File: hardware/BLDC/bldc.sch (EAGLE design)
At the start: 83 parts, among them J1 PWR_2_XT30PW-M, J2 LINEAR_35040500391, J3 LINEAR_8530480810, U1 MA702, U10 MCP2542FD, U11 LDFM33PUR, U2 DRV8323RS, U3 TPN7R006PL, U4 TPN7R006PL, U5 TPN7R006PL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

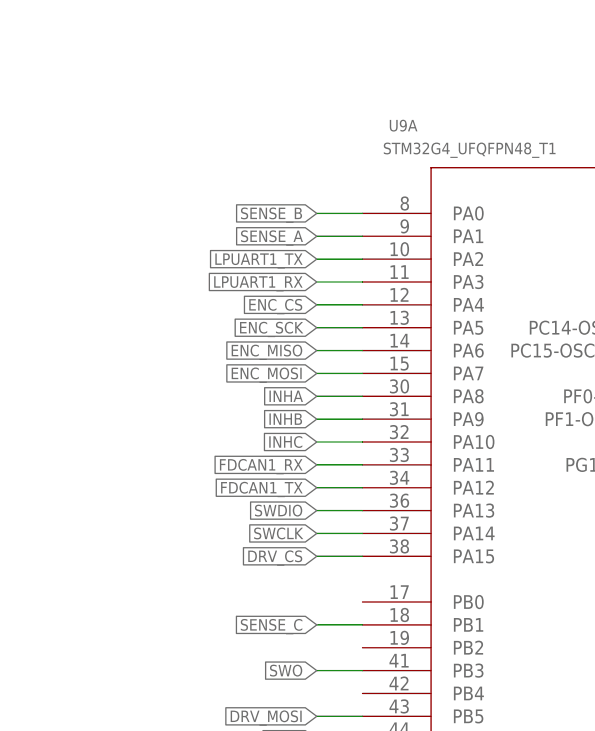
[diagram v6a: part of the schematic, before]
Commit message: Add pullups to SPI NSS pins
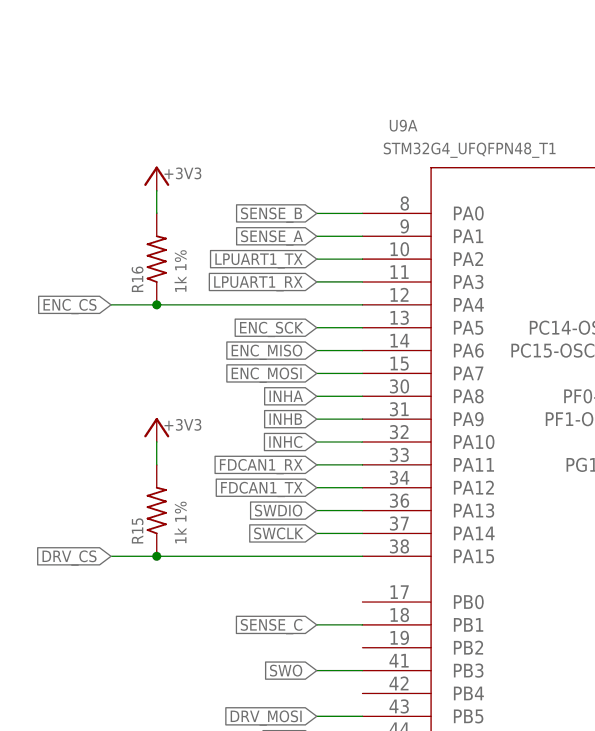
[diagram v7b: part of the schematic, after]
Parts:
- added R15, R16: 1k 1%, _T_rcl:R0402
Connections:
- net +3V3: now also R15.2, R16.2
- net DRV_CS: now also R15.1
- net ENC_CS: now also R16.1
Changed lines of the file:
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@@
 <part name="C43" library="_T_rcl" library_urn="urn:adsk.eagle:library:19571919" deviceset="C" device="0402" package3d_urn="urn:adsk.eagle:package:19572013/4" value="0.1uF 10V"/>
 <part name="GND31" library="_T_power" library_urn="urn:adsk.eagle:library:19572085" deviceset="GND" device=""/>
+<part name="R15" library="_T_rcl" library_urn="urn:adsk.eagle:library:19571919" deviceset="R" device="0402" package3d_urn="urn:adsk.eagle:package:19572014/3" value="1k 1%"/>
+<part name="+3V6" library="_T_power" library_urn="urn:adsk.eagle:library:19572085" deviceset="+3V3" device=""/>
+<part name="R16" library="_T_rcl" library_urn="urn:adsk.eagle:library:19571919" deviceset="R" device="0402" package3d_urn="urn:adsk.eagle:package:19572014/3" value="1k 1%"/>
+<part name="+3V7" library="_T_power" library_urn="urn:adsk.eagle:library:19572085" deviceset="+3V3" device=""/>
 </parts>
 <sheets>
@@
 </instance>
 <instance part="GND31" gate="G$1" x="17.78" y="-20.32" smashed="yes" grouprefs="UCPOWER"/>
+<instance part="R15" gate="G$1" x="-81.28" y="91.44" smashed="yes" rot="R90">
+<attribute name="NAME" x="-82.7786" y="87.63" size="1.27" layer="95" rot="R90"/>
+<attribute name="VALUE" x="-77.978" y="87.63" size="1.27" layer="96" rot="R90"/>
+</instance>
+<instance part="+3V6" gate="G$1" x="-81.28" y="101.6" smashed="yes">
+<attribute name="VALUE" x="-76.2" y="101.6" size="1.27" layer="96" rot="R180"/>
+</instance>
+<instance part="R16" gate="G$1" x="-81.28" y="119.38" smashed="yes" rot="R90">
+<attribute name="NAME" x="-82.7786" y="115.57" size="1.27" layer="95" rot="R90"/>
+<attribute name="VALUE" x="-77.978" y="115.57" size="1.27" layer="96" rot="R90"/>
+</instance>
+<instance part="+3V7" gate="G$1" x="-81.28" y="129.54" smashed="yes">
+<attribute name="VALUE" x="-76.2" y="129.54" size="1.27" layer="96" rot="R180"/>
+</instance>
 </instances>
 <busses>
@@
 <junction x="17.78" y="-7.62" grouprefs="UCPOWER"/>
 </segment>
+<segment>
+<wire x1="-81.28" y1="99.06" x2="-81.28" y2="96.52" width="0.1524" layer="91"/>
+<pinref part="+3V6" gate="G$1" pin="+3V3"/>
+<pinref part="R15" gate="G$1" pin="2"/>
+</segment>
+<segment>
+<wire x1="-81.28" y1="127" x2="-81.28" y2="124.46" width="0.1524" layer="91"/>
+<pinref part="+3V7" gate="G$1" pin="+3V3"/>
+<pinref part="R16" gate="G$1" pin="2"/>
+</segment>
 </net>
 <net name="N$1" class="0">
@@
 <segment>
 <pinref part="U9" gate="A" pin="PA15"/>
-<wire x1="-58.42" y1="86.36" x2="-63.5" y2="86.36" width="0.1524" layer="91" grouprefs="UC_STM32G4"/>
-<label x="-63.5" y="86.36" size="1.27" layer="95" rot="R180" xref="yes" grouprefs="UC_STM32G4"/>
+<wire x1="-58.42" y1="86.36" x2="-81.28" y2="86.36" width="0.1524" layer="91" grouprefs="UC_STM32G4"/>
+<label x="-86.36" y="86.36" size="1.27" layer="95" rot="R180" xref="yes" grouprefs="UC_STM32G4"/>
+<pinref part="R15" gate="G$1" pin="1"/>
+<wire x1="-81.28" y1="86.36" x2="-86.36" y2="86.36" width="0.1524" layer="91" grouprefs="UC_STM32G4"/>
+<junction x="-81.28" y="86.36"/>
 </segment>
 </net>
@@
 <segment>
 <pinref part="U9" gate="A" pin="PA4"/>
-<wire x1="-58.42" y1="114.3" x2="-63.5" y2="114.3" width="0.1524" layer="91" grouprefs="UC_STM32G4"/>
-<label x="-63.5" y="114.3" size="1.27" layer="95" rot="R180" xref="yes" grouprefs="UC_STM32G4"/>
-</segment>
-</net>
+<wire x1="-58.42" y1="114.3" x2="-81.28" y2="114.3" width="0.1524" layer="91" grouprefs="UC_STM32G4"/>
+<label x="-86.36" y="114.3" size="1.27" layer="95" rot="R180" xref="yes" grouprefs="UC_STM32G4"/>
+<pinref part="R16" gate="G$1" pin="1"/>
+<wire x1="-81.28" y1="114.3" x2="-86.36" y2="114.3" width="0.1524" layer="91" grouprefs="UC_STM32G4"/>
+<junction x="-81.28" y="114.3"/>
+</segment>
+</net>

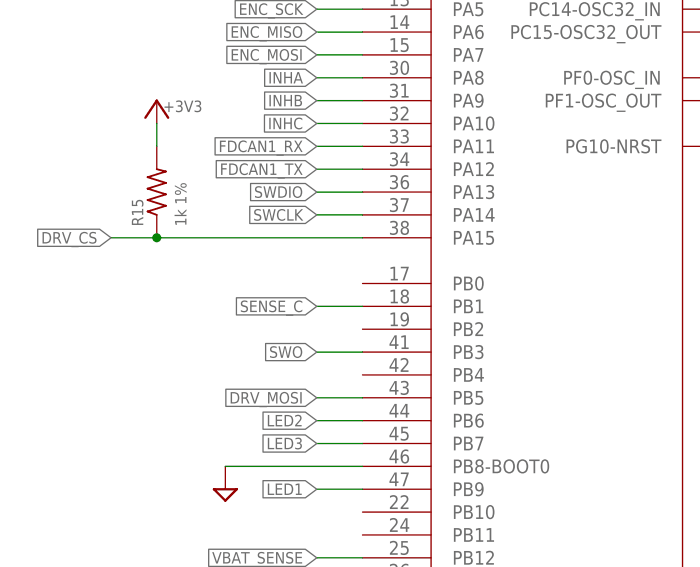
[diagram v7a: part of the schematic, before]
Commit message: Added nfault connection to PB0
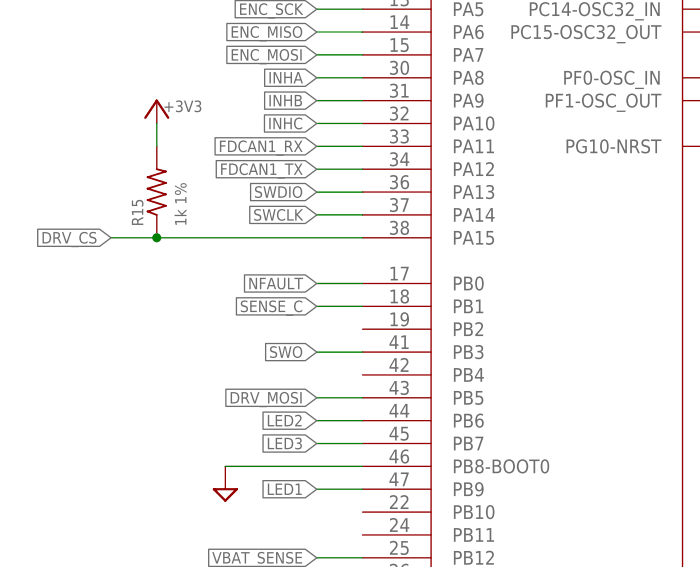
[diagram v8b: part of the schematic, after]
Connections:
- net NFAULT: now also U9A.PB0
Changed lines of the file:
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@@
 <junction x="157.48" y="109.22" grouprefs="GATE_DRIVER_DRV8323RS"/>
+</segment>
+<segment>
+<pinref part="U9" gate="A" pin="PB0"/>
+<wire x1="-58.42" y1="81.28" x2="-63.5" y2="81.28" width="0.1524" layer="91"/>
+<label x="-63.5" y="81.28" size="1.27" layer="95" rot="R180" xref="yes"/>
 </segment>
 </net>
